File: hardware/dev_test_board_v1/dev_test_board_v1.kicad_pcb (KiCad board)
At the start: 2 copper layers, 0 parts

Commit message: Started PCB layout.
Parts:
- added C1: 10n, Capacitor_SMD:C_0603_1608Metric, F.Cu at (195.0, 102.0)
- added C10: 100n, Capacitor_SMD:C_0402_1005Metric, F.Cu at (217.5, 96.0)
- added C11: 1u, Capacitor_SMD:C_0402_1005Metric, F.Cu at (207.0, 91.0)
- added C12: 100n, Capacitor_SMD:C_0402_1005Metric, F.Cu at (208.5, 91.0)
- added C13: 6p, Capacitor_SMD:C_0402_1005Metric, F.Cu at (199.0, 88.0)
- added C14: 6p, Capacitor_SMD:C_0402_1005Metric, F.Cu at (199.0, 82.5)
- added C15: 10u, Capacitor_SMD:C_0402_1005Metric, F.Cu at (228.5, 101.5)
- added C16: 100n, Capacitor_SMD:C_0402_1005Metric, F.Cu at (227.0, 101.5)
- added C17: 100n, Capacitor_SMD:C_0402_1005Metric, F.Cu at (226.5, 99.5)
- added C18: 0.1u, Capacitor_SMD:C_0603_1608Metric, F.Cu at (263.5, 95.0)
- added C19: 0.1u, Capacitor_SMD:C_0603_1608Metric, F.Cu at (262.0, 84.5)
- added C2: 4.7u, Capacitor_SMD:CP_Elec_4x5.4, F.Cu at (205.8, 99.2)
- added C20: 0.1u, Capacitor_SMD:C_0603_1608Metric, F.Cu at (260.5, 74.0)
- added C3: 100n, Capacitor_SMD:C_0402_1005Metric, F.Cu at (206.0, 103.8)
- added C4: 100n, Capacitor_SMD:C_0402_1005Metric, F.Cu at (207.5, 103.2)
- added C5: 47p, Capacitor_SMD:C_0603_1608Metric, F.Cu at (196.5, 109.0)
- added C6: 47p, Capacitor_SMD:C_0603_1608Metric, F.Cu at (196.5, 106.0)
- added C7: 10u, Capacitor_SMD:C_0402_1005Metric, F.Cu at (212.0, 82.5)
- added C8: 100n, Capacitor_SMD:C_0402_1005Metric, F.Cu at (212.0, 84.0)
- added C9: 100n, Capacitor_SMD:C_0402_1005Metric, F.Cu at (220.5, 87.0)
- added D2: YELLOW, LED_SMD:LED_0603_1608Metric, F.Cu at (223.5, 111.5)
- added D3: GREEN, LED_SMD:LED_0603_1608Metric, F.Cu at (223.5, 113.5)
- added D4: RED, LED_SMD:LED_0603_1608Metric, F.Cu at (224.5, 88.0)
- added D5: BLUE, LED_SMD:LED_0603_1608Metric, F.Cu at (224.5, 90.0)
- added FB1: 600R @ 100MHz, Inductor_SMD:L_0805_2012Metric, F.Cu at (198.5, 102.5)
- added H1: MountingHole_Pad, MountingHole:MountingHole_2.7mm_M2.5_Pad_Via, F.Cu at (269.0, 27.0)
- added H2: MountingHole_Pad, MountingHole:MountingHole_2.7mm_M2.5_Pad_Via, F.Cu at (263.5, 18.0)
- added H3: MountingHole_Pad, MountingHole:MountingHole_2.7mm_M2.5_Pad_Via, F.Cu at (279.5, 32.5)
- added H4: MountingHole_Pad, MountingHole:MountingHole_2.7mm_M2.5_Pad_Via, F.Cu at (279.0, 18.0)
- added J1: USB_B_Micro, Connector_USB:USB_Micro-B_GCT_USB3076-30-A, F.Cu at (189.0, 106.5)
- added J2: Conn_SWD, Connector_PinHeader_1.27mm:PinHeader_2x05_P1.27mm_Vertical, F.Cu at (234.5, 72.5)
- added J3: Conn_LCD, Connector_PinSocket_2.54mm:PinSocket_1x08_P2.54mm_Vertical, F.Cu at (209.0, 125.5)
- added J4: Conn_GP, Connector_PinHeader_2.54mm:PinHeader_1x12_P2.54mm_Vertical, F.Cu at (227.5, 68.0)
- added L1: 27n, Inductor_SMD:L_0603_1608Metric, F.Cu at (204.5, 91.5)
- added R1: 27R, Resistor_SMD:R_0402_1005Metric, F.Cu at (199.5, 108.5)
- added R10: 22R, Resistor_SMD:R_0402_1005Metric, F.Cu at (238.5, 70.5)
- added R2: 27R, Resistor_SMD:R_0402_1005Metric, F.Cu at (199.5, 106.5)
- added R3: 270R, Resistor_SMD:R_0603_1608Metric, F.Cu at (219.5, 111.5)
- added R4: 270R, Resistor_SMD:R_0603_1608Metric, F.Cu at (219.5, 113.5)
- added R5: 10k, Resistor_SMD:R_0402_1005Metric, F.Cu at (265.0, 106.5)
- added R6: 1k, Resistor_SMD:R_0603_1608Metric, F.Cu at (228.0, 88.0)
- added R7: 1k, Resistor_SMD:R_0603_1608Metric, F.Cu at (228.0, 90.0)
- added R8: 4R7, Resistor_SMD:R_0402_1005Metric, F.Cu at (221.0, 101.5)
- added R9: 4R7, Resistor_SMD:R_0402_1005Metric, F.Cu at (223.0, 98.0)
- added SW1: SW_SPDT, Button_Switch_SMD:SW_SPDT_PCM12, F.Cu at (272.5, 106.0)
- added SW2: SW_PUSH, Button_Switch_SMD:SW_Push_1P1T_NO_6x6mm_H9.5mm, F.Cu at (272.0, 95.0)
- added SW3: SW_PUSH, Button_Switch_SMD:SW_Push_1P1T_NO_6x6mm_H9.5mm, F.Cu at (270.0, 84.0)
- added SW4: SW_PUSH, Button_Switch_SMD:SW_Push_1P1T_NO_6x6mm_H9.5mm, F.Cu at (268.5, 73.5)
- added U1: STM32L031C4Tx, Package_QFP:LQFP-48_7x7mm_P0.5mm, F.Cu at (214.5, 90.0)
- added U2: FT230XS, Package_SO:SSOP-16_3.9x4.9mm_P0.635mm, F.Cu at (206.0, 108.0)
- added U3: LIS2HH12, Package_LGA:LGA-12_2x2mm_P0.5mm, F.Cu at (225.0, 101.5)
- added Y1: 8MHz, tyjba_footprints:Crystal_NX8045GB, F.Cu at (203.0, 84.5)

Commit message: Draft layout complete.
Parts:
- SW1: footprint Button_Switch_SMD:SW_SPDT_PCM12 -> tyjba_footprints:SW_Unknown_SPDT_Straight
- moved H3 125.9 mm to (193.8, 124.8)
- moved H4 111.3 mm to (247.5, 124.8)
- moved H2 86.4 mm to (193.8, 69.0)
- moved SW1 83.8 mm to (193.8, 77.2), turned to 90 degrees
- moved R5 73.7 mm to (197.2, 77.5)
- moved H1 47.2 mm to (247.5, 69.0)
- moved C18 28.9 mm to (236.2, 104.8)
- moved SW2 28.9 mm to (244.8, 104.8)
- moved C19 27.3 mm to (236.8, 94.8)
- moved SW3 27.3 mm to (244.8, 94.2)
- moved C20 25.9 mm to (236.8, 84.2)
- moved SW4 25.9 mm to (244.8, 83.8)
- moved J1 24.7 mm to (204.5, 125.8), turned to 0 degrees
- moved R10 19.1 mm to (224.5, 83.5)
- moved C1 14.2 mm to (200.0, 115.2), turned to 180 degrees
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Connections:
- J3 pad 1: LCD_LED -> +3V3
- J3 pad 2: SPI1_SCK -> GND
- J3 pad 3: SPI1_MOSI -> LCD_CS
- J3 pad 4: LCD_A0 -> LCD_RST
- J3 pad 5: LCD_RST -> LCD_A0
- J3 pad 6: LCD_CS -> SPI1_MOSI
- J3 pad 7: GND -> SPI1_SCK
- J3 pad 8: +3V3 -> LCD_LED
- U1 pad 14: LCD_LED -> LCD_CS
- U1 pad 18: LCD_A0 -> LCD_RST
- U1 pad 19: LCD_RST -> LCD_A0
- U1 pad 20: LCD_CS -> LCD_LED
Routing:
- added copper zone on In2.Cu, net +3V3
- added copper zone on In1.Cu, net GND
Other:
- board outline added: 61.8 x 63.8 mm
- copper layers 2 -> 4

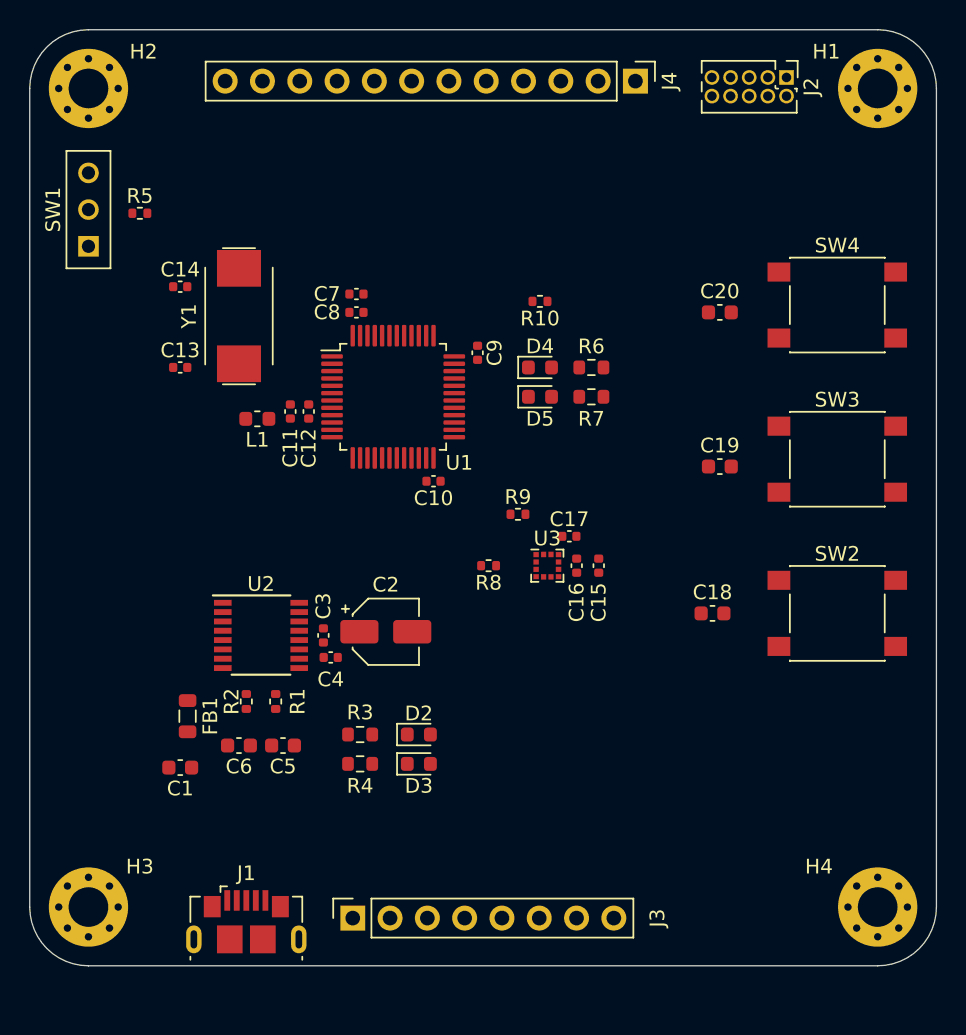
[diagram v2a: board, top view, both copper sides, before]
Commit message: All signals routed.
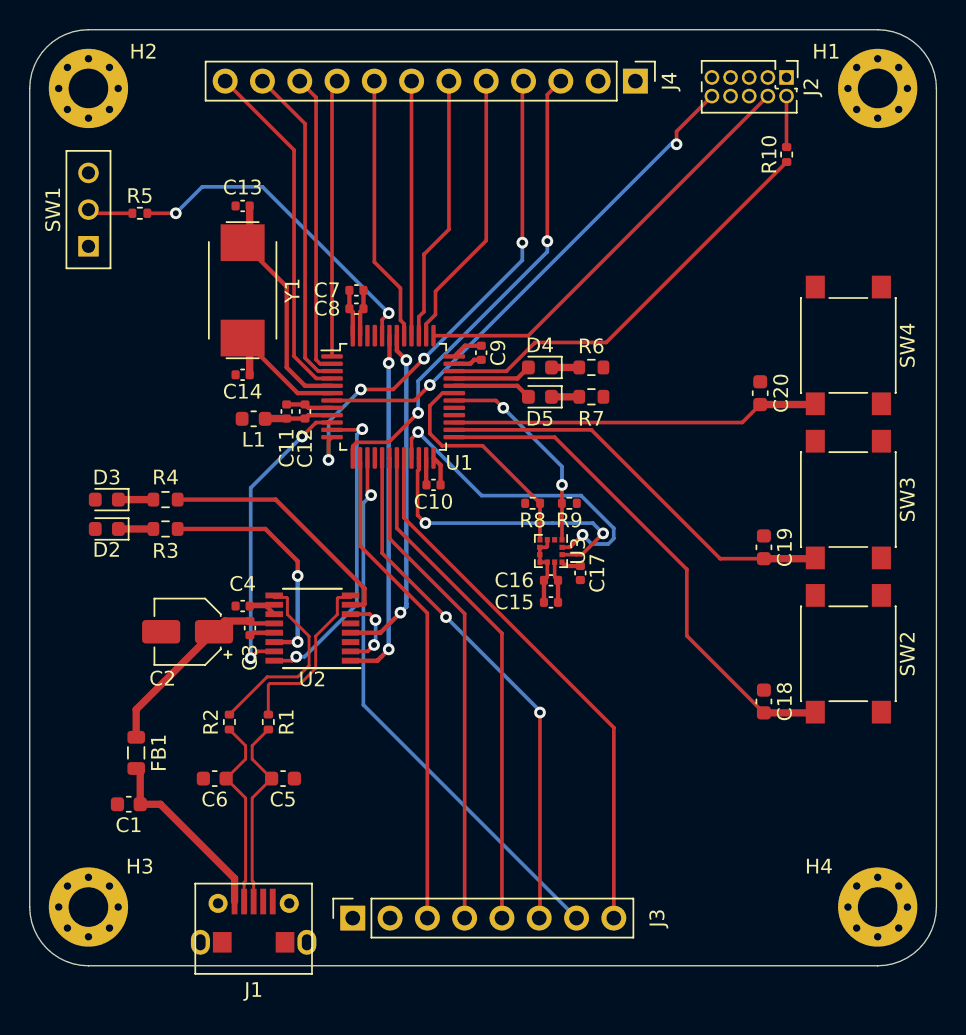
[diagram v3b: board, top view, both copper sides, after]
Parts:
- J1: footprint Connector_USB:USB_Micro-B_GCT_USB3076-30-A -> tyjba_footprints:UBS_Micro-B_Citzends_Aliexpress
- moved D3 27.8 mm to (195.0, 97.0), turned to 180 degrees
- moved D2 25.4 mm to (195.0, 99.0), turned to 180 degrees
- moved R4 22.4 mm to (199.0, 97.0), turned to 0 degrees
- moved R10 19.6 mm to (241.3, 73.5), turned to 90 degrees
- moved R3 19.3 mm to (199.0, 99.0), turned to 0 degrees
- moved C2 13.5 mm to (200.5, 106.0), turned to 180 degrees
- moved C13 11.8 mm to (204.2, 77.0), turned to 180 degrees
- moved C14 7.35 mm to (204.2, 88.5), turned to 180 degrees
- moved C18 6.95 mm to (239.8, 110.8), turned to 270 degrees
- moved C4 6.95 mm to (204.2, 104.2), turned to 180 degrees
- moved C19 6.26 mm to (239.8, 100.2), turned to 270 degrees
- moved C20 6.15 mm to (239.5, 89.8), turned to 270 degrees
- moved R8 5.20 mm to (224.0, 97.2)
- moved C3 5.02 mm to (204.8, 105.8), turned to 270 degrees
- moved C1 4.30 mm to (196.5, 117.8)
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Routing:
- net SPI1_SCK: track 0.00 -> 37.7 mm, vias 0 -> 1
- net LCD_LED: track 0.00 -> 37.3 mm
- net SPI1_MOSI: track 0.00 -> 35.8 mm, vias 0 -> 2
- net SW_GP1: track 0.00 -> 35.0 mm
- net NRST: track 0.00 -> 35.0 mm, vias 0 -> 2
- net LCD_A0: track 0.00 -> 34.3 mm
- net LPUART1_TX: track 0.00 -> 34.2 mm, vias 0 -> 4
- net LCD_RST: track 0.00 -> 33.5 mm
- net LCD_CS: track 0.00 -> 33.2 mm
- net LPUART1_RX: track 0.00 -> 32.8 mm, vias 0 -> 2
- net SW_CLK: track 0.00 -> 29.5 mm
- net SW_DIO: track 0.00 -> 28.5 mm
- net SW_GP2: track 0.00 -> 28.2 mm
- net SW_GP3: track 0.00 -> 25.1 mm
- net USART2_RX: track 0.00 -> 24.3 mm, vias 0 -> 2
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
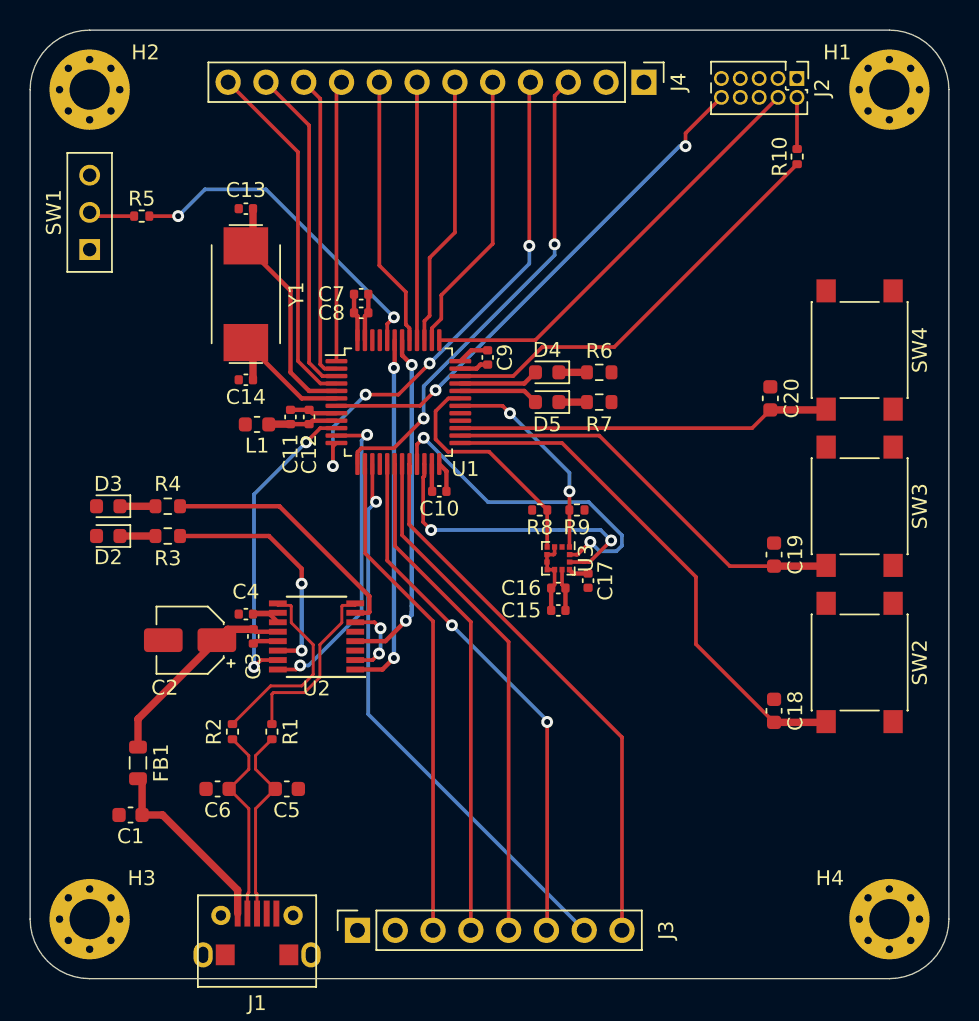
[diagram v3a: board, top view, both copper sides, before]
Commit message: Removed HW debouncing for SW2-4, finished routing.
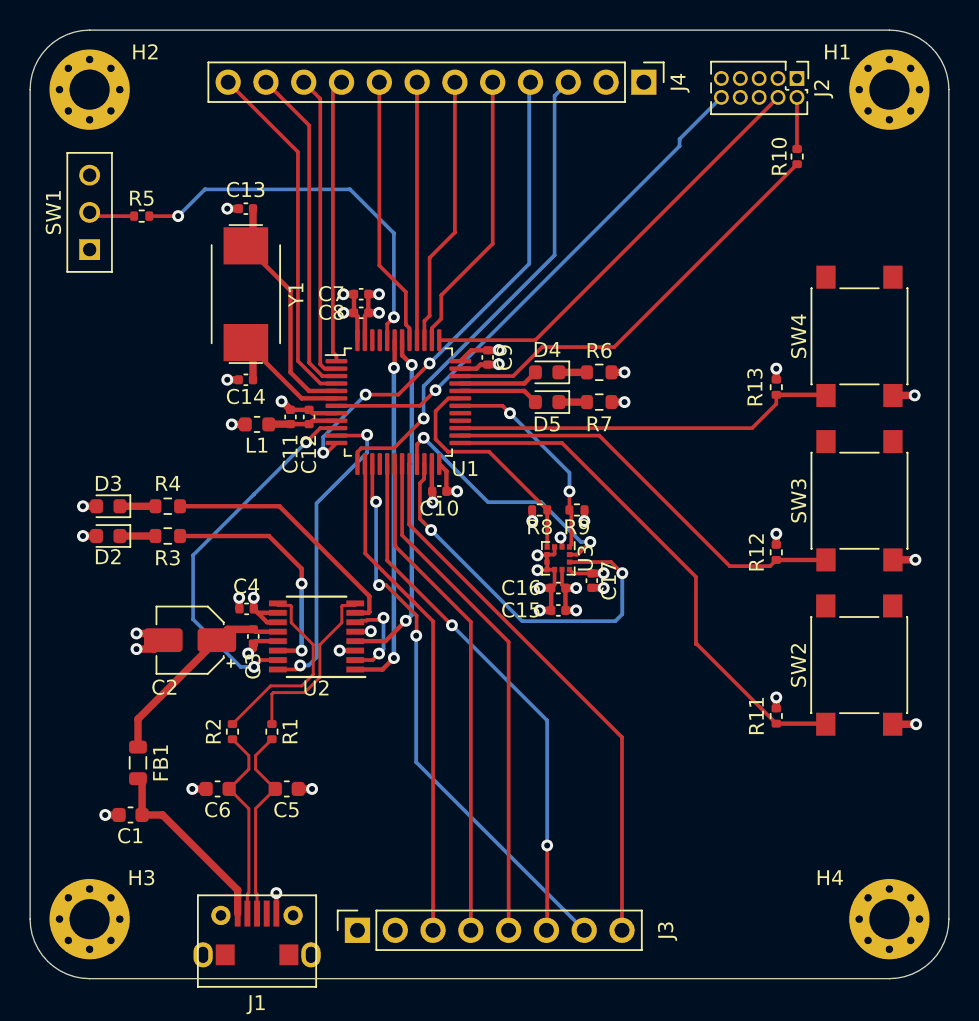
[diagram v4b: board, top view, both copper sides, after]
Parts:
- removed C18, C19, C20: 0.1u, Capacitor_SMD:C_0603_1608Metric
- added R11: 1k, Resistor_SMD:R_0402_1005Metric, F.Cu at (239.9, 111.1)
- added R12: 1k, Resistor_SMD:R_0402_1005Metric, F.Cu at (239.9, 100.1)
- added R13: 1k, Resistor_SMD:R_0402_1005Metric, F.Cu at (239.9, 89.0)
- moved SW4 0.92 mm to (245.5, 85.6), turned to 90 degrees
- moved SW3 0.37 mm to (245.5, 96.6), turned to 90 degrees
- moved C4 0.35 mm to (204.3, 103.9)
- moved C17 0.25 mm to (227.5, 102.0)
- moved SW2 0.18 mm to (245.5, 107.7), turned to 90 degrees
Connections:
- SW2 pad 1: GND -> SW_GP1
- SW2 pad 2: SW_GP1 -> +3V3
- SW3 pad 1: GND -> SW_GP2
- SW3 pad 2: SW_GP2 -> +3V3
- SW4 pad 1: GND -> SW_GP3
- SW4 pad 2: SW_GP3 -> +3V3
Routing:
- net GND: track 17.2 -> 41.0 mm, vias 0 -> 26
- net +3V3: track 15.1 -> 32.0 mm, vias 0 -> 18
- net ACC_INT2: track 20.5 -> 27.1 mm
- net ACC_INT1: track 23.0 -> 17.8 mm
- net USB_CBUS0: track 20.8 -> 24.7 mm
- net BOOT0: track 22.5 -> 25.8 mm
- net Net-(U2-Pad2): track 5.39 -> 6.47 mm
- net LPUART1_TX: track 34.2 -> 33.2 mm, vias 4 -> 3
- net SW_GP3: track 25.1 -> 25.9 mm
- net GPIO4: track 18.9 -> 19.6 mm
- net NRST: track 35.0 -> 34.7 mm, vias 2 -> 1
- net SPI1_SCK: track 37.7 -> 37.5 mm, vias 1 -> 3
- net LPUART1_RX: vias 2 -> 1

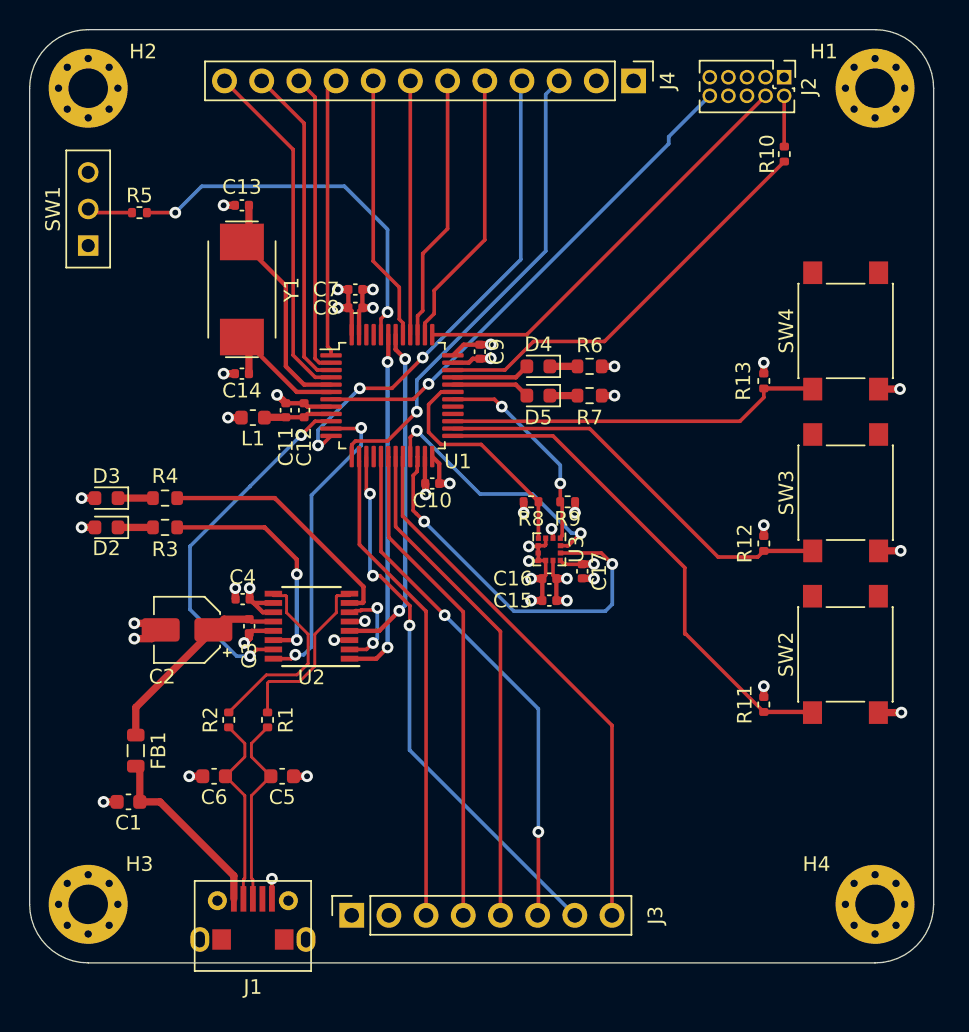
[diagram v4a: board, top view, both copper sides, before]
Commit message: Fixed via placement errors. Added silkscreen for annotations.
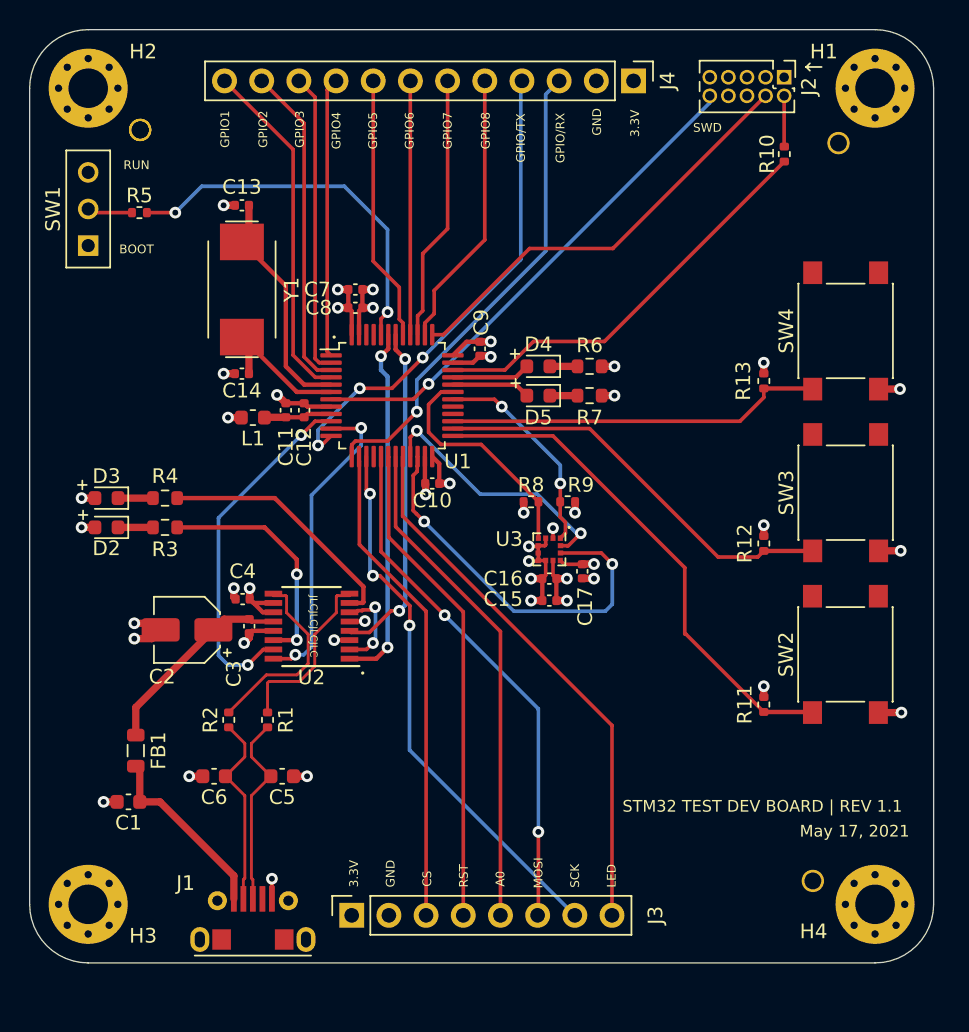
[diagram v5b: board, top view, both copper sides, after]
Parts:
- added REF**: Tooling_Hole-JLCPCB, tyjba_footprints:Tooling_Hole-JLCPCB, F.Cu at (243.2, 123.2)
- added REF** (x2): Tooling_Hole-JLCPCB, tyjba_footprints:Tooling_Hole-JLCPCB, F.Cu at (197.3, 71.8)
- added REF**: Tooling_Hole-JLCPCB, tyjba_footprints:Tooling_Hole-JLCPCB, F.Cu at (245.0, 72.8)
- moved C9 0.20 mm to (220.5, 86.8)
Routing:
- net GPIO4: track 19.6 -> 20.4 mm
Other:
- board text added: "3.3V"
- board text added: "A0"
- board text added: "BOOT"
- board text added: "CS"
- board text added: "GND"
- board text added: "GPIO/RX"
- board text added: "GPIO/TX"
- board text added: "GPIO1"
- board text added: "GPIO2"
- board text added: "GPIO3"
- board text added: "GPIO4"
- board text added: "GPIO5"
- board text added: "GPIO6"
- board text added: "GPIO7"
- board text added: "GPIO8"
- board text added: "JLCJLCJLCJLC"
- board text added: "LED"
- board text added: "MOSI"
- board text added: "May 17, 2021"
- board text added: "RST"
- board text added: "RUN"
- board text added: "SCK"
- board text added: "STM32 TEST DEV BOARD | REV 1.1"
- board text added: "SWD"

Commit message: Routing cleaned up a bit and PCBs ordered.
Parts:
- R1, R2: footprint Resistor_SMD:R_0402_1005Metric -> Resistor_SMD:R_0603_1608Metric
- moved C5 0.85 mm to (207.0, 116.8)
- moved C6 0.85 mm to (202.3, 116.8)
- moved R1 0.85 mm to (206.0, 113.0)
- moved R2 0.85 mm to (203.3, 113.0)
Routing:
- net USB_CONN_D-: track 13.3 -> 12.1 mm
- net USB_CONN_D+: track 13.3 -> 12.1 mm
